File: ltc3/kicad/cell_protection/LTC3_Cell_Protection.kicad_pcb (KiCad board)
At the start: 4 copper layers, 70 parts, among them P1 S2BPHKS, P2 PIN_HEAD_1x2, P3 CONN_BATT_MAIN, P4 CONN_BATT_SENSE, Q1 SUM110P08-11, Q2 SUM110P08-11, Q3 NDS9407, Q4 SUM110P08-11, Q5 SUM110P08-11, Q6 MMBT3904, U1 BQ77PL900, U2 LTC2990

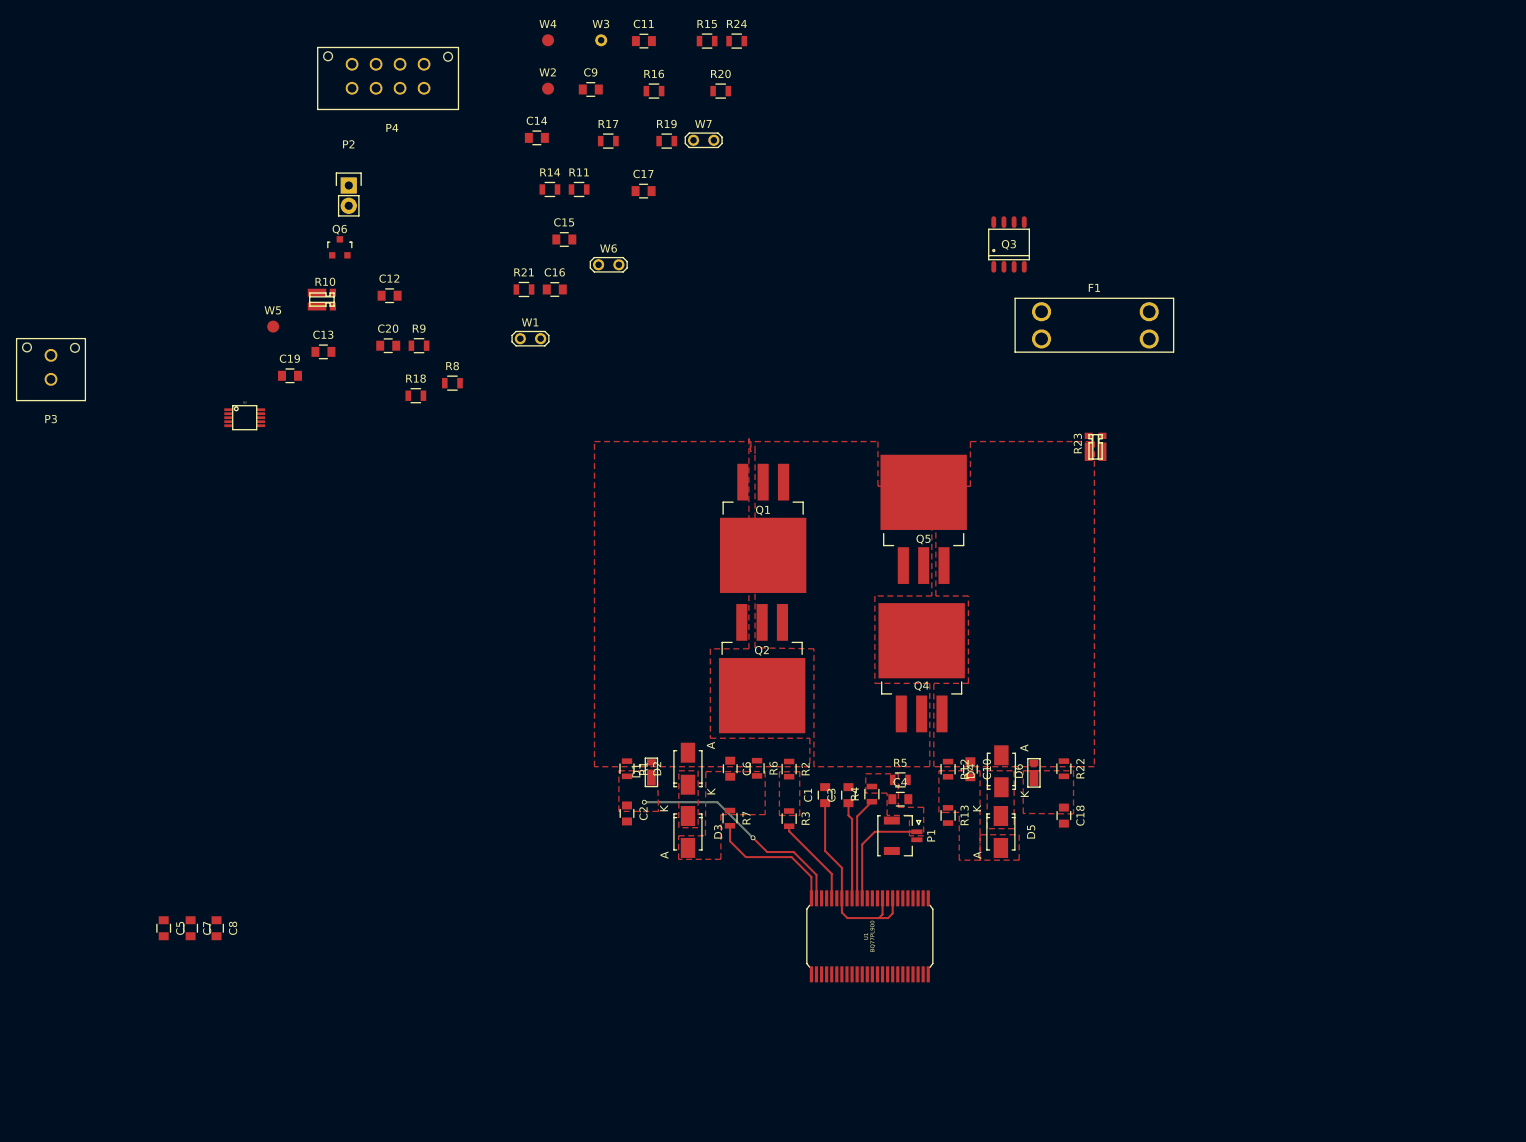
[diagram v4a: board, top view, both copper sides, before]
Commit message: LTC3: Cell Protection Layout
Made significant progress of Cell Protection board layout,
connected most nodes and began creating ground planes.

Reorganized mounting holes on Charge Controller
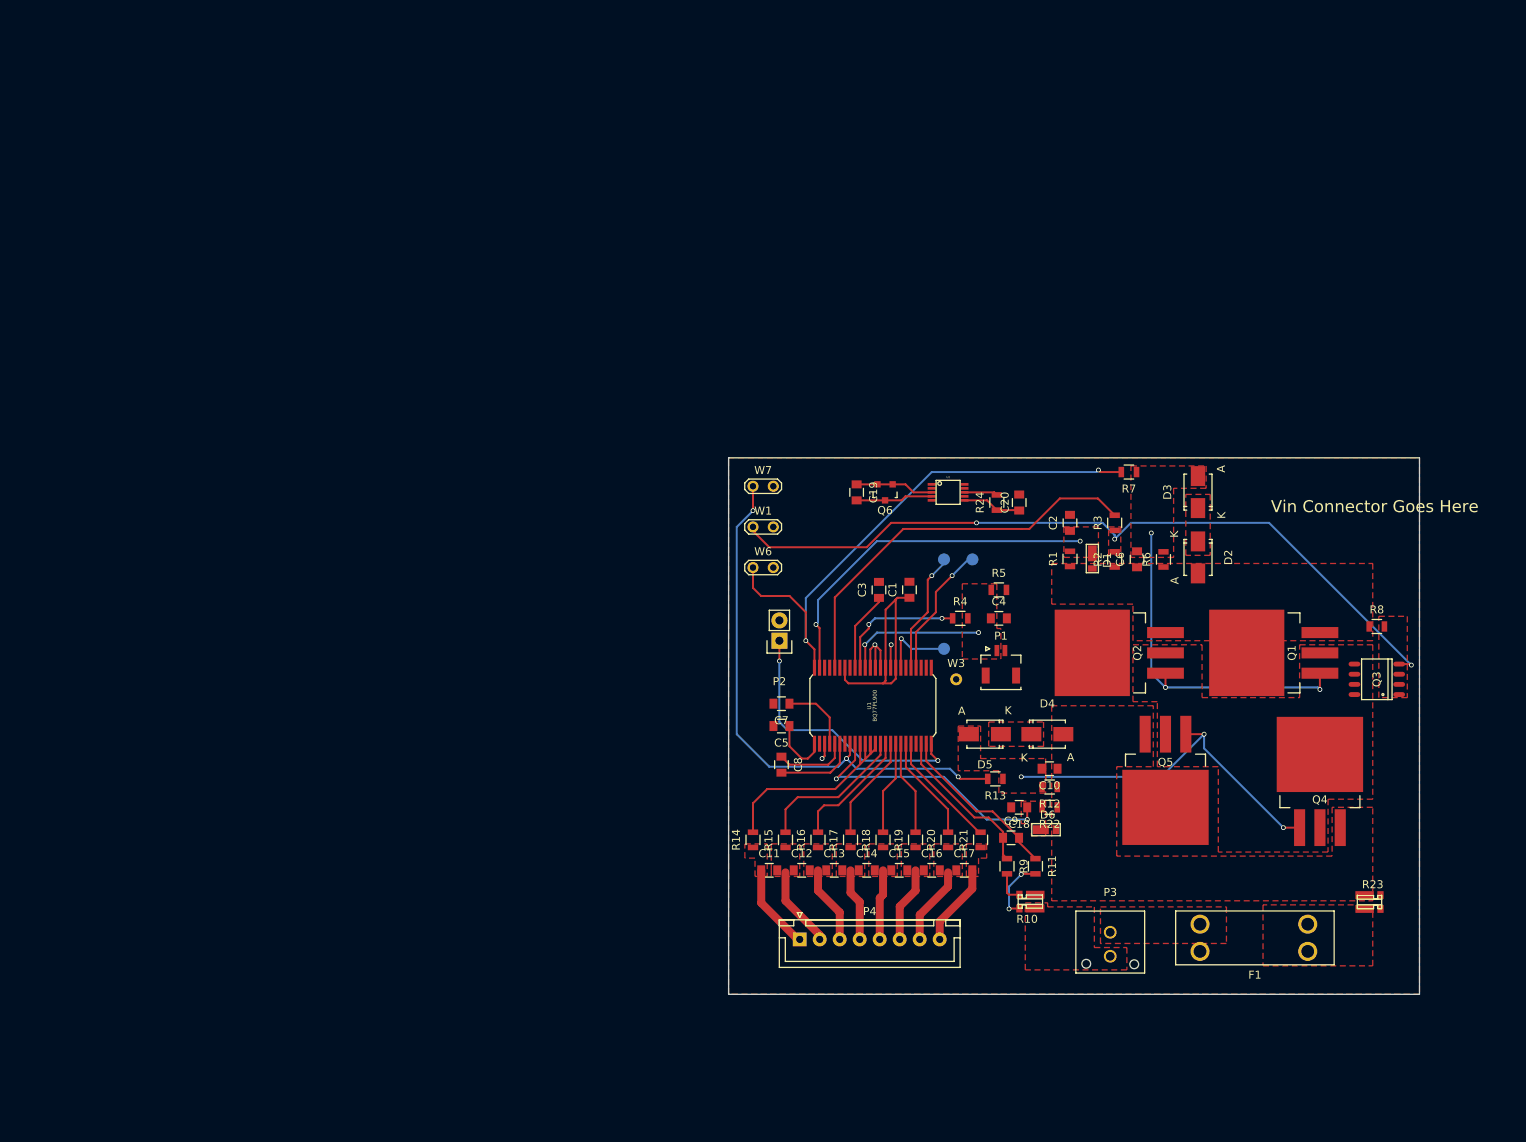
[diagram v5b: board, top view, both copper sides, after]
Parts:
- P3: value CONN_BATT_MAIN -> Micro Fit header, vert.
- P4: value CONN_BATT_SENSE -> XH header, straight; footprint Connectors_Molex:Molex_Microfit3_Header_02x04_Straight_43045-0828 -> Connectors_JST:JST_XH_B08B-XH-A_08x2.50mm_Straight
- W2, W4, W5: moved to B.Cu
- moved P3 149.4 mm to (153.4, 125.9), turned to 180 degrees
- moved R8 119.5 mm to (186.7, 87.6)
- moved P4 116.3 mm to (114.6, 126.7)
- moved R10 116.1 mm to (144.0, 121.2), turned to 180 degrees
- moved C9 107.3 mm to (141.0, 114.0)
- moved C11 104.8 mm to (110.7, 118.1)
- moved R11 102.0 mm to (144.0, 117.6), turned to 270 degrees
- moved C14 100.4 mm to (122.9, 118.1)
- moved R15 100.3 mm to (112.8, 114.3), turned to 90 degrees
- moved R9 98.2 mm to (140.5, 117.6), turned to 270 degrees
- moved R20 97.8 mm to (133.1, 114.3), turned to 90 degrees
- moved R16 95.8 mm to (116.8, 114.3), turned to 90 degrees
- moved C17 93.9 mm to (135.1, 118.1)
- moved R19 92.7 mm to (129.0, 114.3), turned to 90 degrees
- moved R17 92.4 mm to (120.9, 114.3), turned to 90 degrees
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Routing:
- net Net-(Q3-Pad4): track 0.00 -> 95.8 mm, vias 0 -> 3
- net Net-(R13-Pad2): track 0.00 -> 68.4 mm, vias 0 -> 3
- net Net-(R7-Pad2): track 16.6 -> 69.3 mm, vias 0 -> 2
- net Net-(C10-Pad2): track 0.00 -> 45.2 mm, vias 0 -> 3
- net Net-(C6-Pad2): track 0.00 -> 43.3 mm, vias 0 -> 3
- net Net-(R3-Pad2): track 11.2 -> 49.8 mm
- net Net-(P2-Pad1): track 0.00 -> 34.4 mm, vias 0 -> 2
- net Net-(C18-Pad1): track 0.00 -> 33.1 mm, vias 0 -> 2
- net Net-(R14-Pad2): track 0.00 -> 28.1 mm
- net Net-(C9-Pad2): track 0.00 -> 21.2 mm
- net Net-(C9-Pad1): track 0.00 -> 19.9 mm
- net Net-(R15-Pad2): track 0.00 -> 19.0 mm
- net Net-(U1-Pad28): track 0.00 -> 16.8 mm, vias 0 -> 1
- net Net-(C2-Pad1): track 28.2 -> 44.6 mm
- net Net-(R16-Pad2): track 0.00 -> 15.6 mm
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- added copper zone on F.Cu, net GND
- added copper zone on Ground_Plane, net GND
- added copper zone on F.Cu, net Net-(C11-Pad1)
- added copper zone on F.Cu, net Net-(C11-Pad2)
- added copper zone on F.Cu, net Net-(C12-Pad2)
- added copper zone on F.Cu, net Net-(C13-Pad2)
- added copper zone on F.Cu, net Net-(C14-Pad2)
- added copper zone on F.Cu, net Net-(C15-Pad2)
- added copper zone on F.Cu, net Net-(C16-Pad2)
- added copper zone on F.Cu, net Net-(C17-Pad2)
- added copper zone on F.Cu, net Net-(F1-Pad1)
- added copper zone on F.Cu, net Net-(F1-Pad2)
- added copper zone on F.Cu, net Net-(P3-Pad2)
- added copper zone on F.Cu, net Net-(Q3-Pad1)
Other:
- board outline added: 86.4 x 67.1 mm
- board text added: "Vin Connector Goes Here"

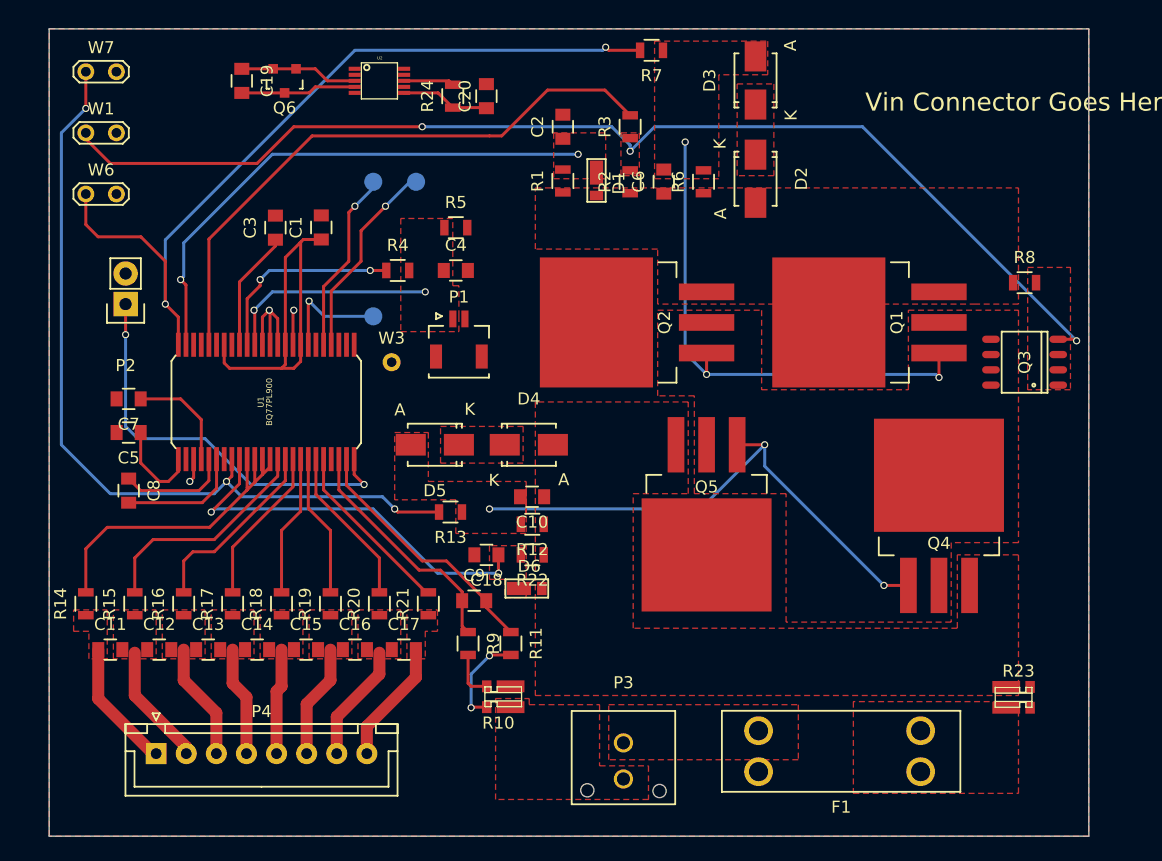
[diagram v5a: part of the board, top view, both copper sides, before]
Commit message: LTC3: Cell Protection Layout
Finished prelimiary Cell Protection Layout.  All nodes connected, mounting
holes on.  Still to do:

	-Check connector P1 (should it be surface mount?)
	-Add Vin connector
	-Find some way to give 5V to LTC2990
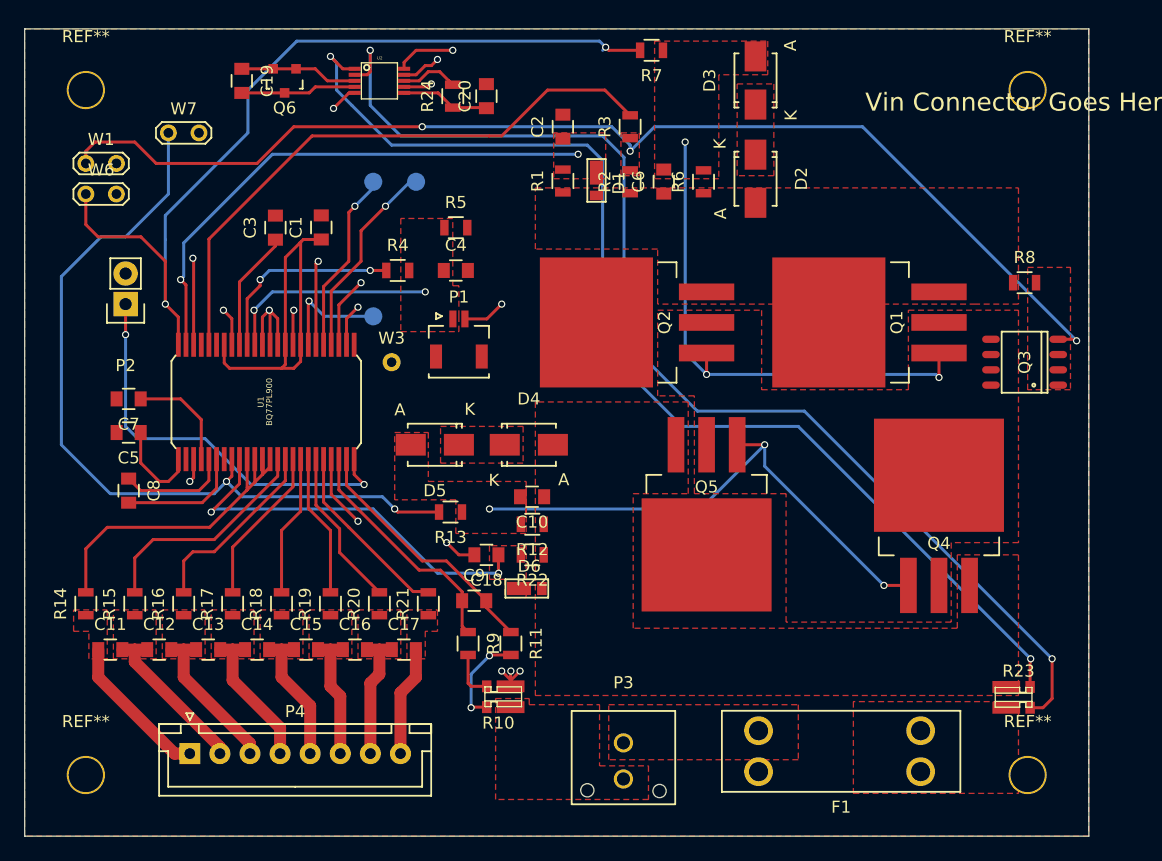
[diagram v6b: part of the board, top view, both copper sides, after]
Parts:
- added REF**: MountingHole_0.1120in_#4, LTC3:MountingHole_0.1120in_number4, F.Cu at (186.9, 128.5)
- added REF**: MountingHole_0.1120in_#4, LTC3:MountingHole_0.1120in_number4, F.Cu at (108.7, 71.6)
- added REF**: MountingHole_0.1120in_#4, LTC3:MountingHole_0.1120in_number4, F.Cu at (186.9, 71.6)
- added REF**: MountingHole_0.1120in_#4, LTC3:MountingHole_0.1120in_number4, F.Cu at (108.7, 128.5)
- moved W7 8.53 mm to (115.6, 75.2)
- moved P4 2.79 mm to (117.3, 126.7)
- moved W1 2.54 mm to (108.7, 77.7)
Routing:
- net Net-(R23-Pad3): track 0.00 -> 97.6 mm, vias 0 -> 2
- net Net-(R23-Pad4): track 0.00 -> 94.1 mm, vias 0 -> 2
- net GND: track 14.0 -> 52.9 mm, vias 3 -> 14
- net /I2C_DATA: track 0.00 -> 33.1 mm, vias 0 -> 2
- net /I2C_CLOCK: track 0.00 -> 31.1 mm, vias 0 -> 2
- net Net-(R7-Pad2): track 69.3 -> 73.3 mm
- net Net-(C11-Pad2): track 10.2 -> 13.6 mm
- net Net-(C13-Pad2): track 9.11 -> 12.3 mm
- net Net-(C12-Pad2): track 9.76 -> 13.0 mm
- net Net-(C14-Pad2): track 8.81 -> 11.7 mm
- net Net-(C11-Pad1): track 10.8 -> 12.5 mm
- net Net-(C15-Pad2): track 9.46 -> 11.0 mm
- net Net-(C16-Pad2): track 9.85 -> 11.0 mm
- net Net-(C17-Pad2): track 10.3 -> 9.17 mm
- net Net-(R24-Pad2): track 4.18 -> 5.27 mm
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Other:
- board size 86.4 x 67.1 mm -> 88.4 x 67.1 mm

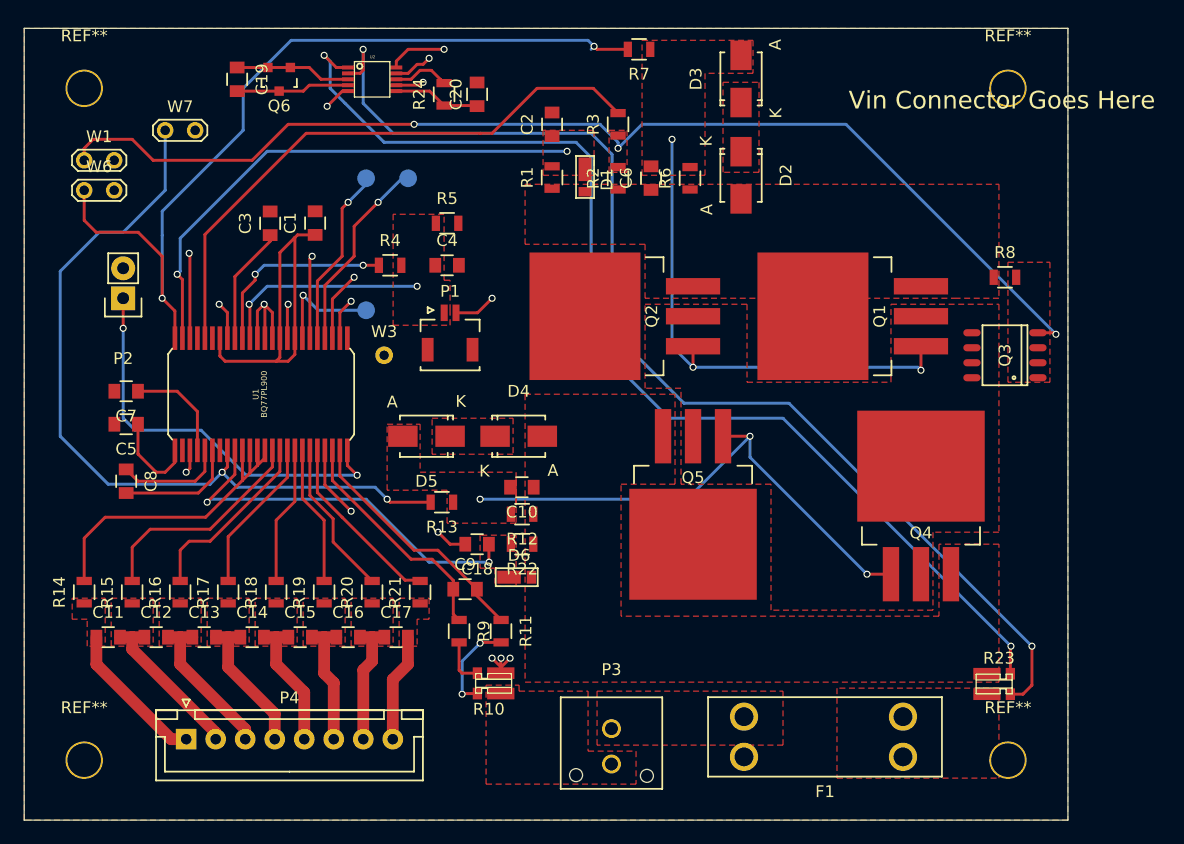
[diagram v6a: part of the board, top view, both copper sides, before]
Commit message: LTC3: Layout Work/Connector Updating
Added many needed connectors and added to layout.

	-Added 5V nodes for Charge Controller/Cell Protection
	-Added I2C bus connectors
	-Added Vin connectors for Cell Protection

Added all connectors to layout and ensured all nodes were connected.
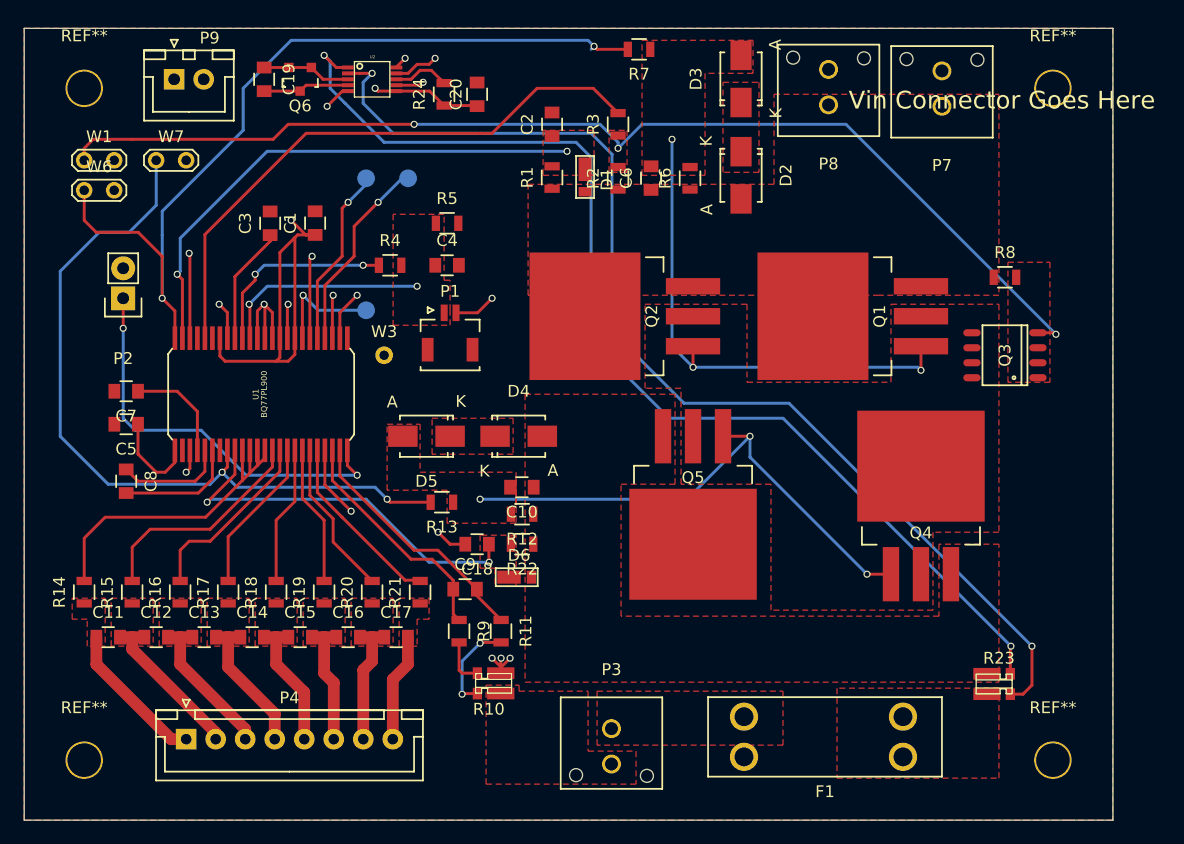
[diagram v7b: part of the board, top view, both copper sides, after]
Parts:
- added P7: MicroFit head., Connectors_Molex:Molex_Microfit3_Header_02x01_Straight_43045-0228, F.Cu at (181.4, 73.2)
- added P8: MicroFit head., Connectors_Molex:Molex_Microfit3_Header_02x01_Straight_43045-0228, F.Cu at (171.8, 73.0)
- added P9: XH header, straight, Connectors_JST:JST_XH_B02B-XH-A_02x2.50mm_Straight, F.Cu at (116.3, 70.9)
- P3: value Micro Fit header, vert. -> MicroFit header
- moved REF** 3.81 mm to (190.8, 128.5)
- moved REF** 3.81 mm to (190.8, 71.6)
- moved W7 2.65 mm to (114.8, 77.7)
- moved C19 2.29 mm to (124.0, 70.9)
- moved Q6 1.78 mm to (127.0, 70.9)
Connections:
- net VBATT renamed /VBATT
- C1 pad 1: Net-(C1-Pad1) -> +5V
- U1 pad 27: /I2C_CLOCK -> /I2C_CLK
- U1 pad 32: Net-(C1-Pad1) -> +5V
- U1 pad 34: Net-(C1-Pad1) -> +5V
- U1 pad 42: Net-(C1-Pad1) -> +5V
- U2 pad 6: /I2C_DATA -> /I2C_CLK
- U2 pad 7: /I2C_CLOCK -> /I2C_DATA
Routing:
- net +5V: track 7.37 -> 57.3 mm, vias 0 -> 2
- net /I2C_CLK: track 0.00 -> 45.1 mm, vias 0 -> 2
- net Net-(C1-Pad1): track 31.2 -> 0.00 mm
- net /I2C_CLOCK: track 31.1 -> 0.00 mm, vias 2 -> 0
- net /I2C_DATA: track 33.1 -> 54.5 mm
- net Net-(R23-Pad3): track 97.6 -> 94.8 mm
- net Net-(R13-Pad2): track 67.3 -> 64.8 mm
- net Net-(C19-Pad2): track 9.59 -> 7.31 mm
- net Net-(C19-Pad1): track 9.80 -> 7.51 mm
- net Net-(Q3-Pad4): track 96.5 -> 95.1 mm
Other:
- board size 88.4 x 67.1 mm -> 92.2 x 67.1 mm
